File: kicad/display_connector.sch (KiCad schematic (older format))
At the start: 1 part, among them J2 Display

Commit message: routing
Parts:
- renumbered J2 to J6
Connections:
- net Fn: now also J6.67 (P67), J6.68 (P68), J6.69 (P69); no longer J6.1 (P1), J6.2 (P2), J6.3 (P3)
- net Fp: now also J6.1 (P1), J6.2 (P2), J6.3 (P3); no longer J6.67 (P67), J6.68 (P68), J6.69 (P69)
- net L4_1: now also J6.27 (P27); no longer J6.33 (P33)
- net L4_2: now also J6.28 (P28); no longer J6.32 (P32)
- net L4_3: now also J6.29 (P29); no longer J6.31 (P31)
- net L4_5: now also J6.31 (P31); no longer J6.29 (P29)
- net L4_6: now also J6.32 (P32); no longer J6.28 (P28)
- net L4_7: now also J6.33 (P33); no longer J6.27 (P27)
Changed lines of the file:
@@
 LIBS:conn
 LIBS:74xx
-LIBS:Relay
 LIBS:custom
 LIBS:vfd_driver-cache
-EELAYER 26 0
+EELAYER 25 0
 EELAYER END
 $Descr A4 11693 8268
 encoding utf-8
-Sheet 3 3
+Sheet 3 11
 Title ""
 Date ""
@@
 $EndDescr
 $Comp
-L CONN_01X69 J2
+L CONN_01X69 J6
 U 1 1 59FF3645
 P 5150 4150
-F 0 "J2" H 5228 4191 50  0000 L CNN
+F 0 "J6" H 5228 4191 50  0000 L CNN
 F 1 "Display" H 5228 4100 50  0000 L CNN
 F 2 "modules:vfd_FUTABA_24-SD-01GK_24x1" H 5150 5850 50  0001 C CNN
@@
 NoConn ~ 4950 7250
 NoConn ~ 4950 7150
+Text HLabel 4250 7450 0    60   Input ~ 0
+Fn
 Text HLabel 4250 850  0    60   Input ~ 0
-Fn
-Text HLabel 4250 7450 0    60   Input ~ 0
 Fp
 Entry Wire Line
@@
 Wire Bus Line
 	2350 1150 2350 4950
-Text Label 2900 3950 0    60   ~ 0
-L4_1
-Text Label 2900 3850 0    60   ~ 0
-L4_2
-Text Label 2900 3750 0    60   ~ 0
-L4_3
-Text Label 2900 3650 0    60   ~ 0
-L4_4
-Text Label 2900 3550 0    60   ~ 0
-L4_5
-Text Label 2900 3450 0    60   ~ 0
-L4_6
-Text Label 2900 3350 0    60   ~ 0
-L4_7
 Text Label 2500 4050 0    60   ~ 0
 L5_1
@@
 Wire Wire Line
 	2450 4650 4950 4650
+Text Label 2950 3350 0    60   ~ 0
+L4_1
+Text Label 2950 3450 0    60   ~ 0
+L4_2
+Text Label 2950 3550 0    60   ~ 0
+L4_3
+Text Label 2950 3650 0    60   ~ 0
+L4_4
+Text Label 2950 3750 0    60   ~ 0
+L4_5
+Text Label 2950 3850 0    60   ~ 0
+L4_6
+Text Label 2950 3950 0    60   ~ 0
+L4_7
 $EndSCHEMATC

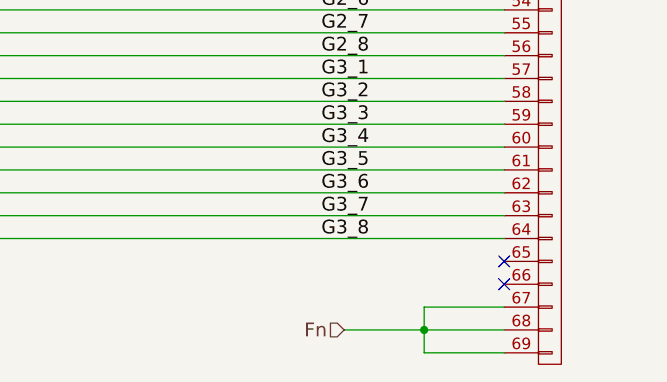
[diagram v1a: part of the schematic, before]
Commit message: Not working need high side driver
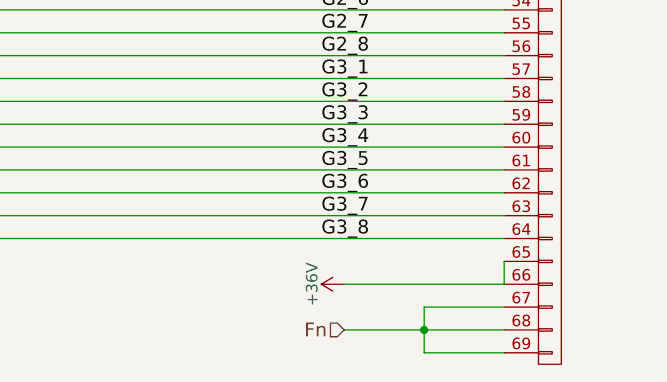
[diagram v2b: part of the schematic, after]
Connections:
- net +36V: now reaches J6.65 (P65)
- net +36V: now also J6.66 (P66)
- no-connect marks 4 -> 2
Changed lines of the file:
@@
 NoConn ~ 4950 1050
 NoConn ~ 4950 1150
-NoConn ~ 4950 7250
-NoConn ~ 4950 7150
 Text HLabel 4250 7450 0    60   Input ~ 0
 Fn
@@
 Text Label 2950 3950 0    60   ~ 0
 L4_7
+Wire Wire Line
+	4950 7150 4950 7250
+Wire Wire Line
+	4950 7250 4250 7250
+$Comp
+L +36V #PWR?
+U 1 1 5A18F7C8
+P 4250 7250
+F 0 "#PWR?" H 4250 7100 50  0001 C CNN
+F 1 "+36V" H 4250 7390 50  0000 C CNN
+F 2 "" H 4250 7250 50  0001 C CNN
+F 3 "" H 4250 7250 50  0001 C CNN
+	1    4250 7250
+	0    -1   -1   0
+$EndComp
 $EndSCHEMATC
